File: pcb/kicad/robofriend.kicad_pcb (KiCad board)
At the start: 2 copper layers, 32 parts, among them J1 Conn_01x20_Female, J10 Pwr_Terminal, J11 Pwr_Terminal, J12 Pwr_Terminal, J13 Conn_02x05, J14 Conn_02x05, J15 Conn_02x05, J2 Conn_01x20_Female, J4 Conn_01x03, J5 Conn_01x02, J6 Conn_01x02, J7 Conn_01x02, J8 Conn_01x02, J9 Pwr_Terminal, U1 Teensy++2.0

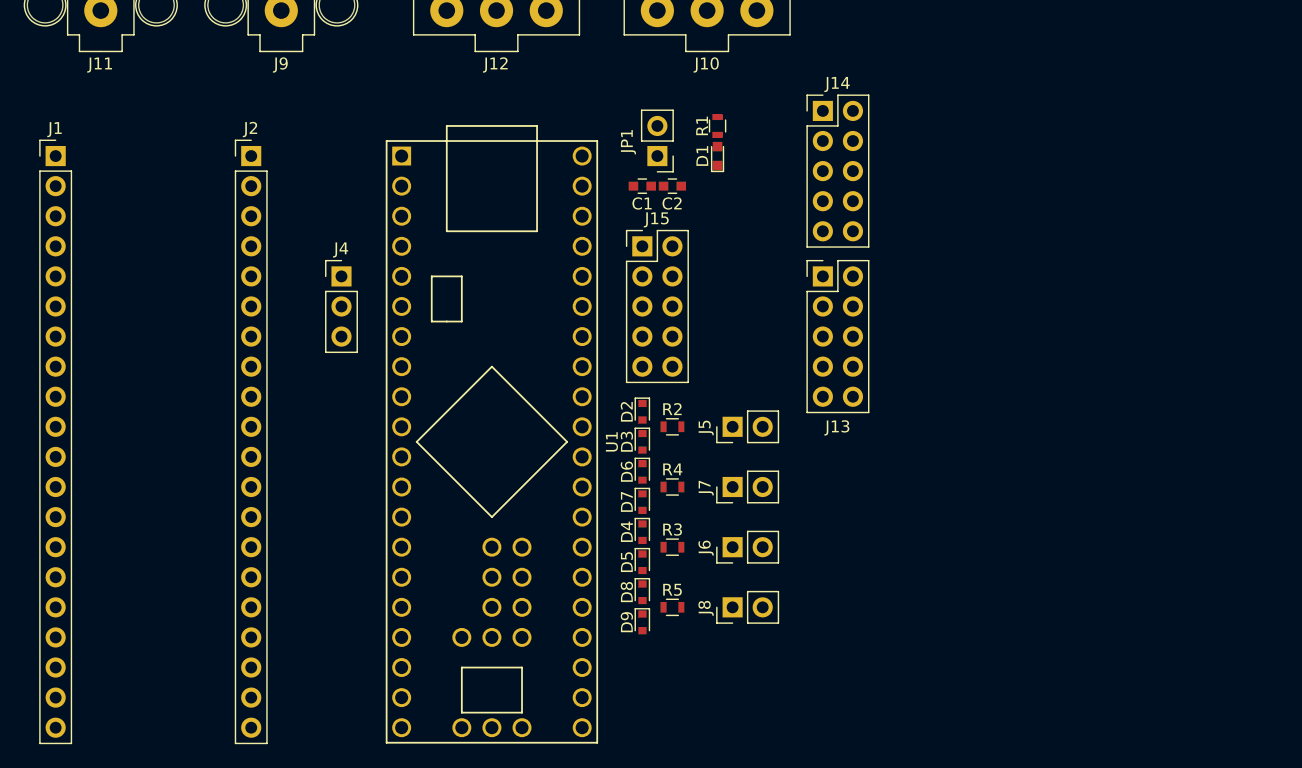
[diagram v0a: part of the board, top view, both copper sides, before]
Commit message: added vin-ver-2 simulation, solved voltage divider complexity
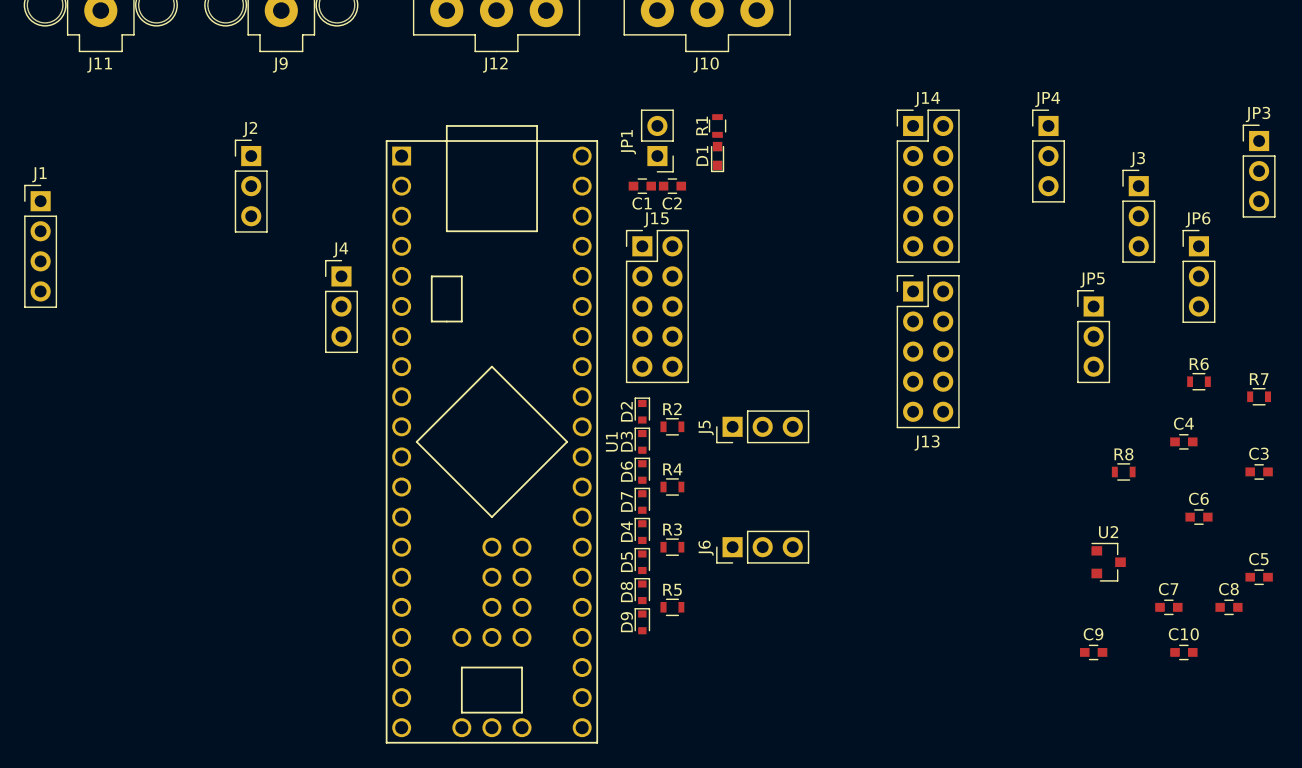
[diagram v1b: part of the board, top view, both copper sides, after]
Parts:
- removed J7, J8: Conn_01x02, Pin_Headers:Pin_Header_Straight_1x02_Pitch2.54mm
- added C10: 100n, Capacitors_SMD:C_0603, F.Cu at (180.3, 153.7)
- added C3: 100n, Capacitors_SMD:C_0603, F.Cu at (186.7, 138.4)
- added C4: 100n, Capacitors_SMD:C_0603, F.Cu at (180.3, 135.9)
- added C5: 100n, Capacitors_SMD:C_0603, F.Cu at (186.7, 147.3)
- added C6: 100n, Capacitors_SMD:C_0603, F.Cu at (181.6, 142.2)
- added C7: 100n, Capacitors_SMD:C_0603, F.Cu at (179.1, 149.9)
- added C8: 100n, Capacitors_SMD:C_0603, F.Cu at (184.2, 149.9)
- added C9: 100n, Capacitors_SMD:C_0603, F.Cu at (172.7, 153.7)
- added J3: ADC2, Pin_Headers:Pin_Header_Straight_1x03_Pitch2.54mm, F.Cu at (176.5, 114.3)
- added JP3: Jumper, Pin_Headers:Pin_Header_Straight_1x03_Pitch2.54mm, F.Cu at (186.7, 110.5)
- added JP4: Jumper, Pin_Headers:Pin_Header_Straight_1x03_Pitch2.54mm, F.Cu at (168.9, 109.2)
- added JP5: Jumper, Pin_Headers:Pin_Header_Straight_1x03_Pitch2.54mm, F.Cu at (172.7, 124.5)
- added JP6: Jumper, Pin_Headers:Pin_Header_Straight_1x03_Pitch2.54mm, F.Cu at (181.6, 119.4)
- added R6: 1.8k, Resistors_SMD:R_0603, F.Cu at (181.6, 130.8)
- added R7: 1.8k, Resistors_SMD:R_0603, F.Cu at (186.7, 132.1)
- added R8: 909, Resistors_SMD:R_0603, F.Cu at (175.3, 138.4)
- added U2: LM4040, TO_SOT_Packages_SMD:SOT-23, F.Cu at (174.0, 146.1)
- J1: value Conn_01x20_Female -> I2C; footprint Socket_Strips:Socket_Strip_Straight_1x20_Pitch2.54mm -> Pin_Headers:Pin_Header_Straight_1x04_Pitch2.54mm
- J15: value Conn_02x05 -> UART
- J2: value Conn_01x20_Female -> ADC1; footprint Socket_Strips:Socket_Strip_Straight_1x20_Pitch2.54mm -> Pin_Headers:Pin_Header_Straight_1x03_Pitch2.54mm
- J4: value Conn_01x03 -> UART
- J5: value Conn_01x02 -> ADC3; footprint Pin_Headers:Pin_Header_Straight_1x02_Pitch2.54mm -> Pin_Headers:Pin_Header_Straight_1x03_Pitch2.54mm
- J6: value Conn_01x02 -> ADC4; footprint Pin_Headers:Pin_Header_Straight_1x02_Pitch2.54mm -> Pin_Headers:Pin_Header_Straight_1x03_Pitch2.54mm
- moved J13 7.73 mm to (157.5, 123.2)
- moved J14 7.73 mm to (157.5, 109.2)
- moved J1 4.02 mm to (83.8, 115.6)
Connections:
- D2 pad 1: +5V -> Net-(D2-Pad1)
- D4 pad 1: +5V -> Net-(D4-Pad1)
- D6 pad 1: +5V -> Net-(D6-Pad1)
- D8 pad 1: +5V -> Net-(D8-Pad1)
- J1 pad 1: Net-(J1-Pad1) -> +5V
- J1 pad 2: Net-(J1-Pad2) -> /D1
- J1 pad 3: Net-(J1-Pad3) -> /D0
- J1 pad 4: Net-(J1-Pad4) -> GND
- J2 pad 1: Net-(J2-Pad1) -> Net-(D2-Pad1)
- J2 pad 3: Net-(J2-Pad3) -> GND
- J5 pad 1: Net-(J5-Pad1) -> Net-(D4-Pad1)
- J5 pad 2: GND -> Net-(J5-Pad2)
- J6 pad 1: Net-(J6-Pad1) -> Net-(D8-Pad1)
- J6 pad 2: GND -> Net-(J6-Pad2)
- R2 pad 2: Net-(J5-Pad1) -> Net-(J2-Pad2)
- R3 pad 2: Net-(J6-Pad1) -> Net-(J5-Pad2)
- R5 pad 2: Net-(J8-Pad1) -> Net-(J6-Pad2)
- U1 pad 32: /VREF -> /AREF

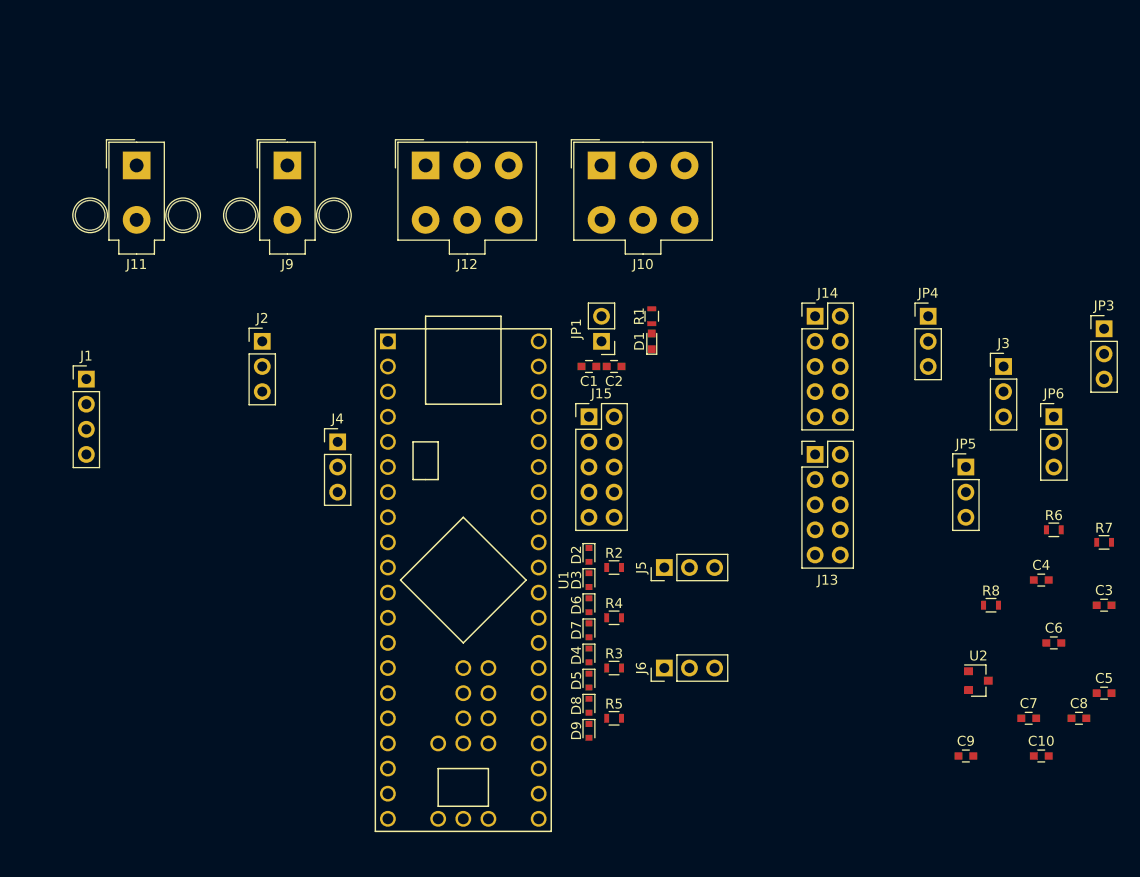
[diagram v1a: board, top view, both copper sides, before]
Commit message: added sla-12vdc lib and footprint to the project
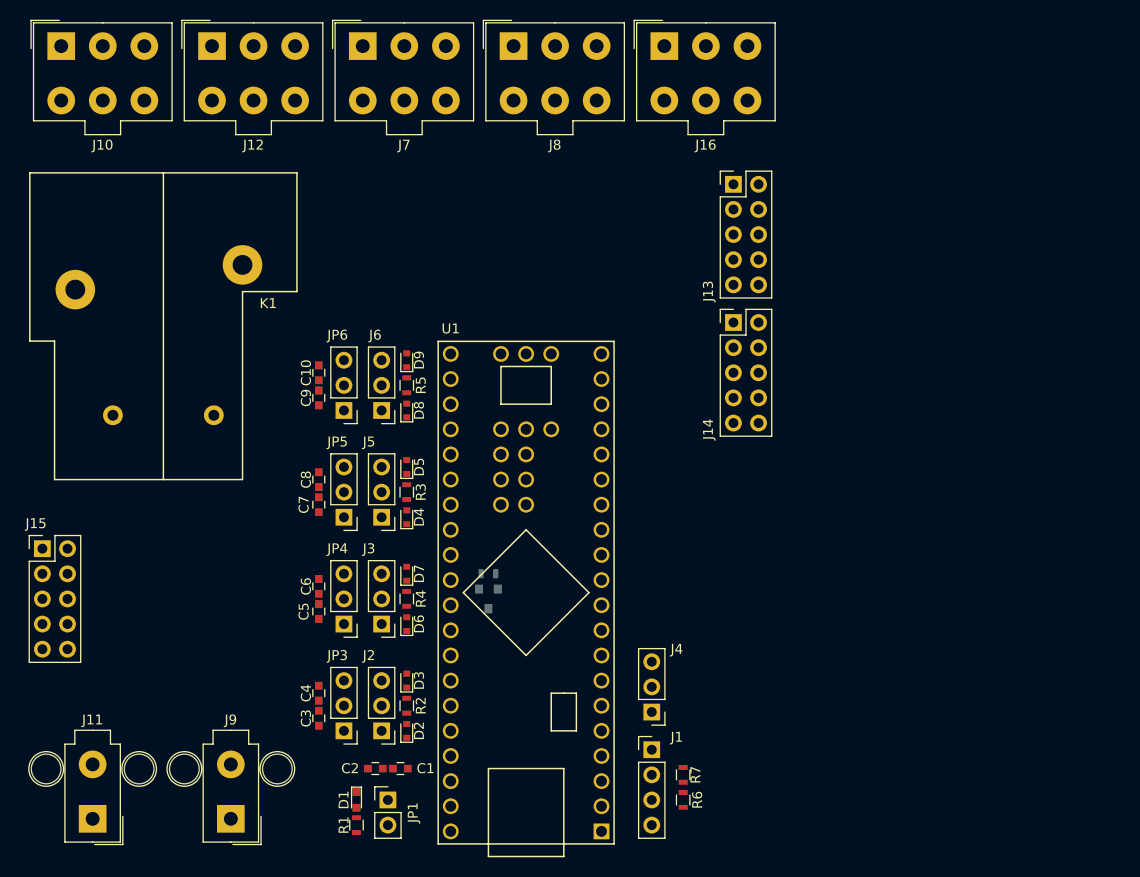
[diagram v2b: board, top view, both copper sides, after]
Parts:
- added J16: AUDIOAMP, Connectors_Molex:Molex_MiniFit-JR-5556-06A_2x03x4.20mm_Straight, F.Cu at (142.2, 81.9)
- added J7: BOOST2, Connectors_Molex:Molex_MiniFit-JR-5556-06A_2x03x4.20mm_Straight, F.Cu at (111.8, 81.9)
- added J8: MONITOR, Connectors_Molex:Molex_MiniFit-JR-5556-06A_2x03x4.20mm_Straight, F.Cu at (127.0, 81.9)
- added K1: SANYOU_SRD_Form_A, SLA_12VDC:SLA-12VDC, F.Cu at (78.1, 125.7)
- J10: value Pwr_Terminal -> VBAT
- J12: value Pwr_Terminal -> BOOST1
- R8, U2: moved to B.Cu
- moved JP3 86.9 mm to (109.9, 151.1), turned to 180 degrees
- moved C10 82.7 mm to (107.3, 114.9), turned to 270 degrees
- moved C8 80.5 mm to (107.3, 125.7), turned to 270 degrees
- moved C3 80.2 mm to (107.3, 149.9), turned to 90 degrees
- moved C5 79.8 mm to (107.3, 139.1), turned to 90 degrees
- moved C7 74.9 mm to (107.3, 128.3), turned to 90 degrees
- moved C9 74.8 mm to (107.3, 117.5), turned to 90 degrees
- moved C6 74.5 mm to (107.3, 136.5), turned to 270 degrees
- moved C4 73.9 mm to (107.3, 147.3), turned to 270 degrees
- moved JP6 71.8 mm to (109.9, 118.7), turned to 180 degrees
- moved J1 68.3 mm to (141.0, 153.0)
- moved J3 68.0 mm to (113.7, 140.3), turned to 180 degrees
- moved JP4 66.8 mm to (109.9, 140.3), turned to 180 degrees
- moved J9 66.3 mm to (98.4, 160.0), turned to 180 degrees
- moved J11 66.2 mm to (84.5, 160.0), turned to 180 degrees
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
